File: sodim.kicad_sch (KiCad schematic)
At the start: 2 parts

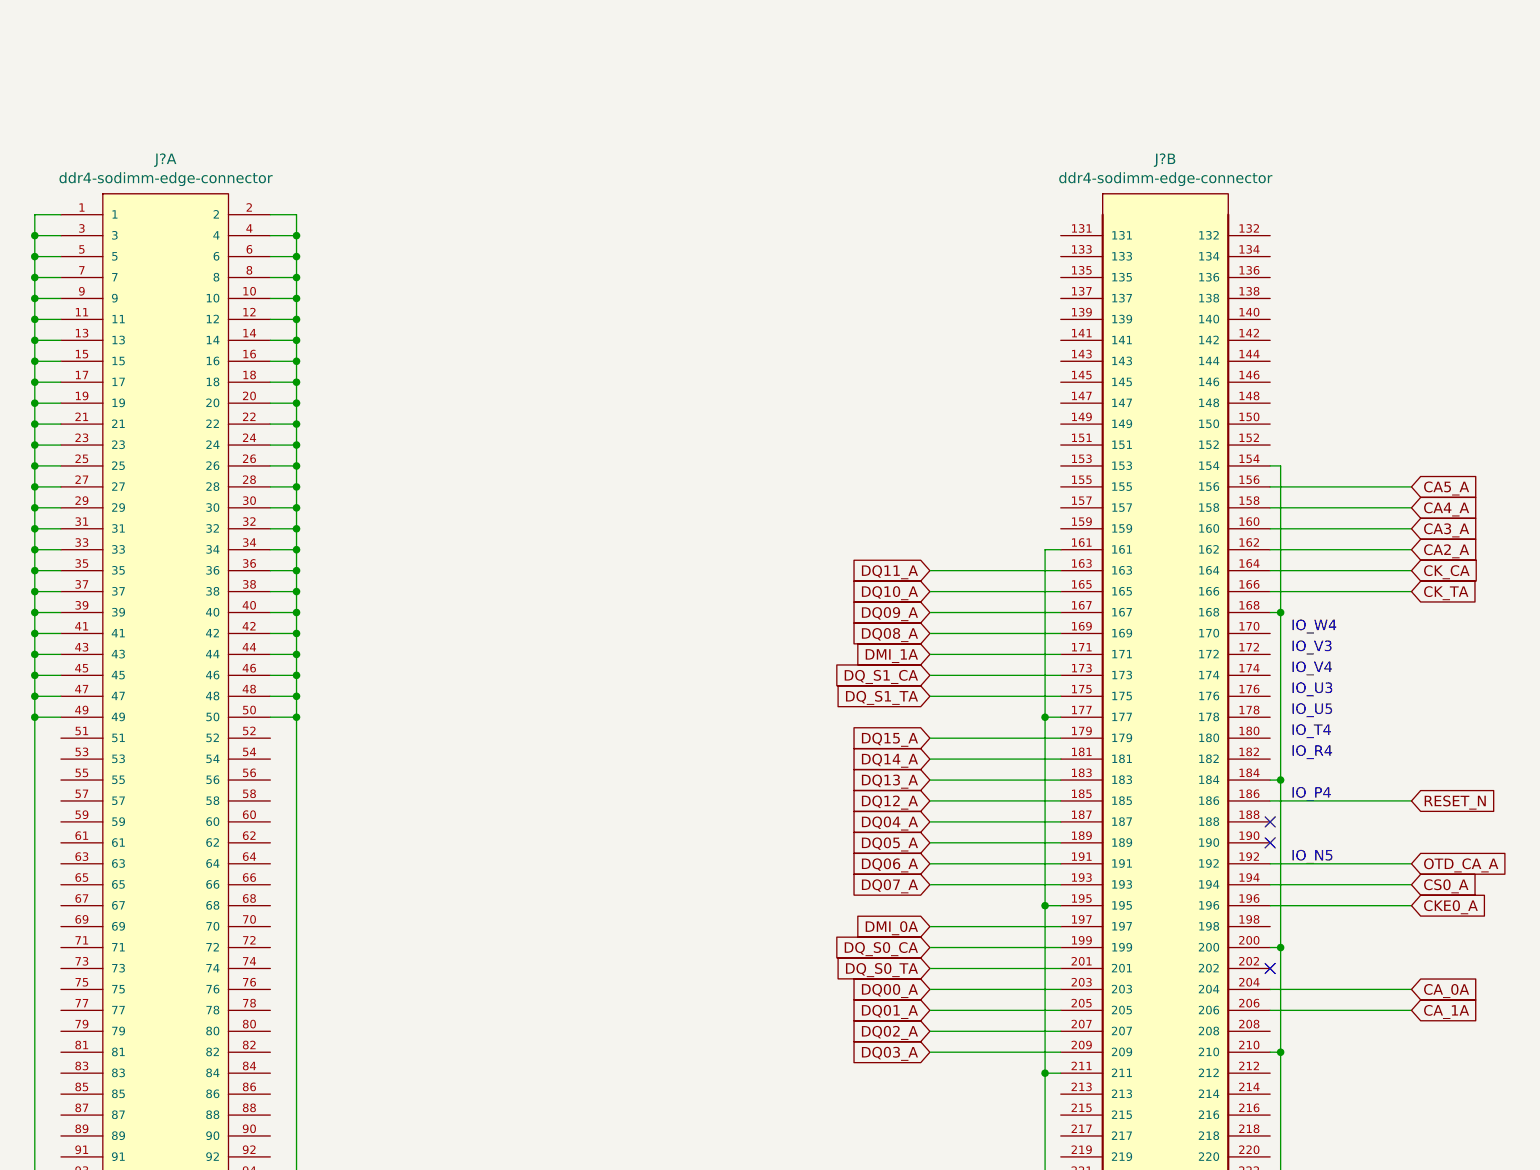
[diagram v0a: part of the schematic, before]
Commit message: Fix net names
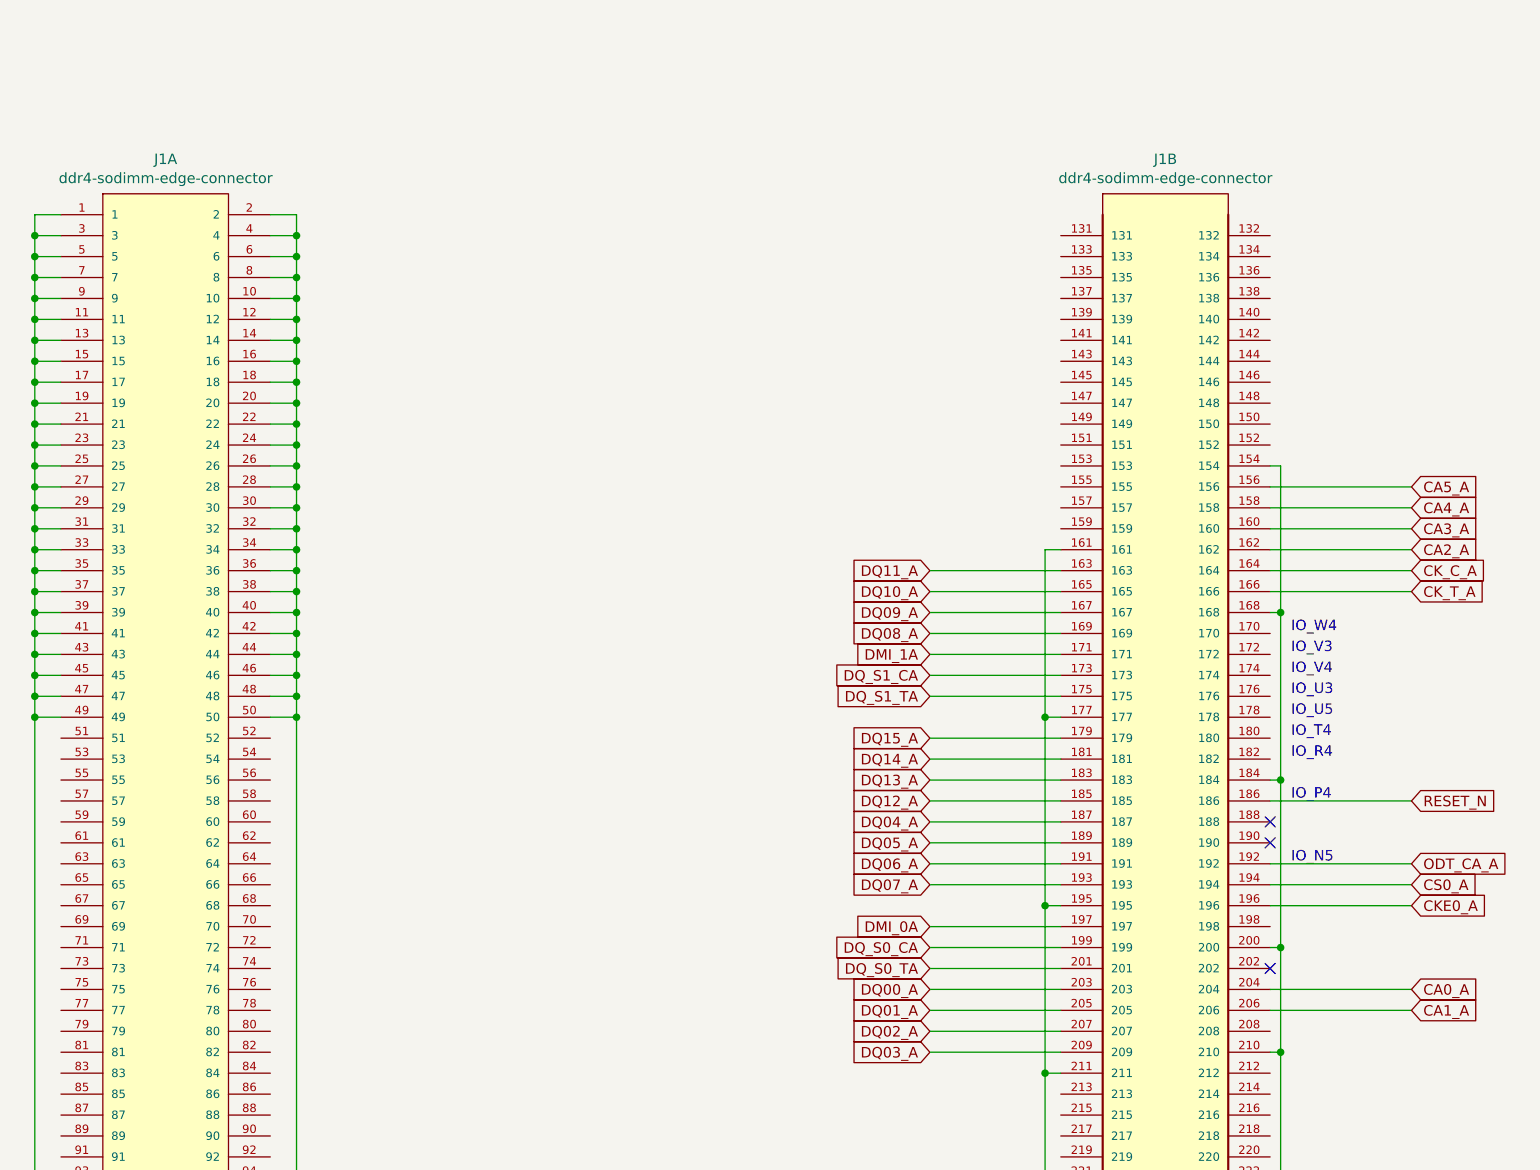
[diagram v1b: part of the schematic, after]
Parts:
- gave numbers to parts that had none: 1
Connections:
- net CA_0A renamed CA0_A
- net CA_1A renamed CA1_A
- net CK_CA renamed CK_C_A
- net CK_TA renamed CK_T_A
- net OTD_CA_A renamed ODT_CA_A

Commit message: Fix missing global links (wip), designators fixed
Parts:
- removed J1: ddr4-sodimm-edge-connector, lpddr4-testbed-footprints:SODIMM_DDR4_EDGE, symbol lpddr4-testbed:ddr4-sodimm-edge-connector
- added J1: Bus_DDR4_Edge_Conn, antmicro-footprints:Bus_DDR4_Conn_Edge, symbol antmicroMemoryConnectorsPCCardSockets:Bus_DDR4_Edge_Conn
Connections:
- net CA0_A: now also J1.204
- net CA1_A: now also J1.206
- net CA2_A: now also J1.162
- net CA3_A: now also J1.160
- net CA4_A: now also J1.158
- net CA5_A: now also J1.156
- net CKE0_A: now also J1.196
- net CK_C_A: now also J1.164
- net CK_T_A: now also J1.166
- net CS0_A: now also J1.194
- net DMI_0A: now also J1.197
- net DMI_1A: now also J1.171
- net DQ00_A: now also J1.203
- net DQ01_A: now also J1.205
- net DQ02_A: now also J1.207
- net DQ03_A: now also J1.209
- net DQ04_A: now also J1.187
- net DQ05_A: now also J1.189
- net DQ06_A: now also J1.191
- net DQ07_A: now also J1.193
- net DQ08_A: now also J1.169
- net DQ09_A: now also J1.167
- net DQ10_A: now also J1.165
- net DQ11_A: now also J1.163
- net DQ12_A: now also J1.185
- net DQ13_A: now also J1.183
- net DQ14_A: now also J1.181
- net DQ15_A: now also J1.179
- net DQ_S0_CA: now also J1.199
- net DQ_S0_TA: now also J1.201
- net DQ_S1_CA: now also J1.173
- net DQ_S1_TA: now also J1.175
- net GND: now also J1.1, J1.10, J1.11, J1.12, J1.13, J1.14, J1.15, J1.154, J1.16, J1.161, J1.168, J1.17, J1.177, J1.18, J1.184, J1.19, J1.195, J1.2, J1.20, J1.200, J1.21, J1.210, J1.211, J1.22, J1.23, J1.24, J1.25, J1.26, J1.27, J1.28, J1.29, J1.3, J1.30, J1.31, J1.32, J1.33, J1.34, J1.35, J1.36, J1.37, J1.38, J1.39, J1.4, J1.40, J1.41, J1.42, J1.43, J1.44, J1.45, J1.46, J1.47, J1.48, J1.49, J1.5, J1.50, J1.6, J1.7, J1.8, J1.9
- net ODT_CA_A: now also J1.192
- net RESET_N: now also J1.186
- net SCL: now also J1.129
- net SDA: now also J1.127
- net VDD1: now also J1.116, J1.118, J1.120, J1.122, J1.124
- net VDD2: now also J1.101, J1.103, J1.105, J1.107, J1.93, J1.95, J1.97, J1.99
- net VDDQ: now also J1.126, J1.128, J1.130, J1.246, J1.248, J1.250

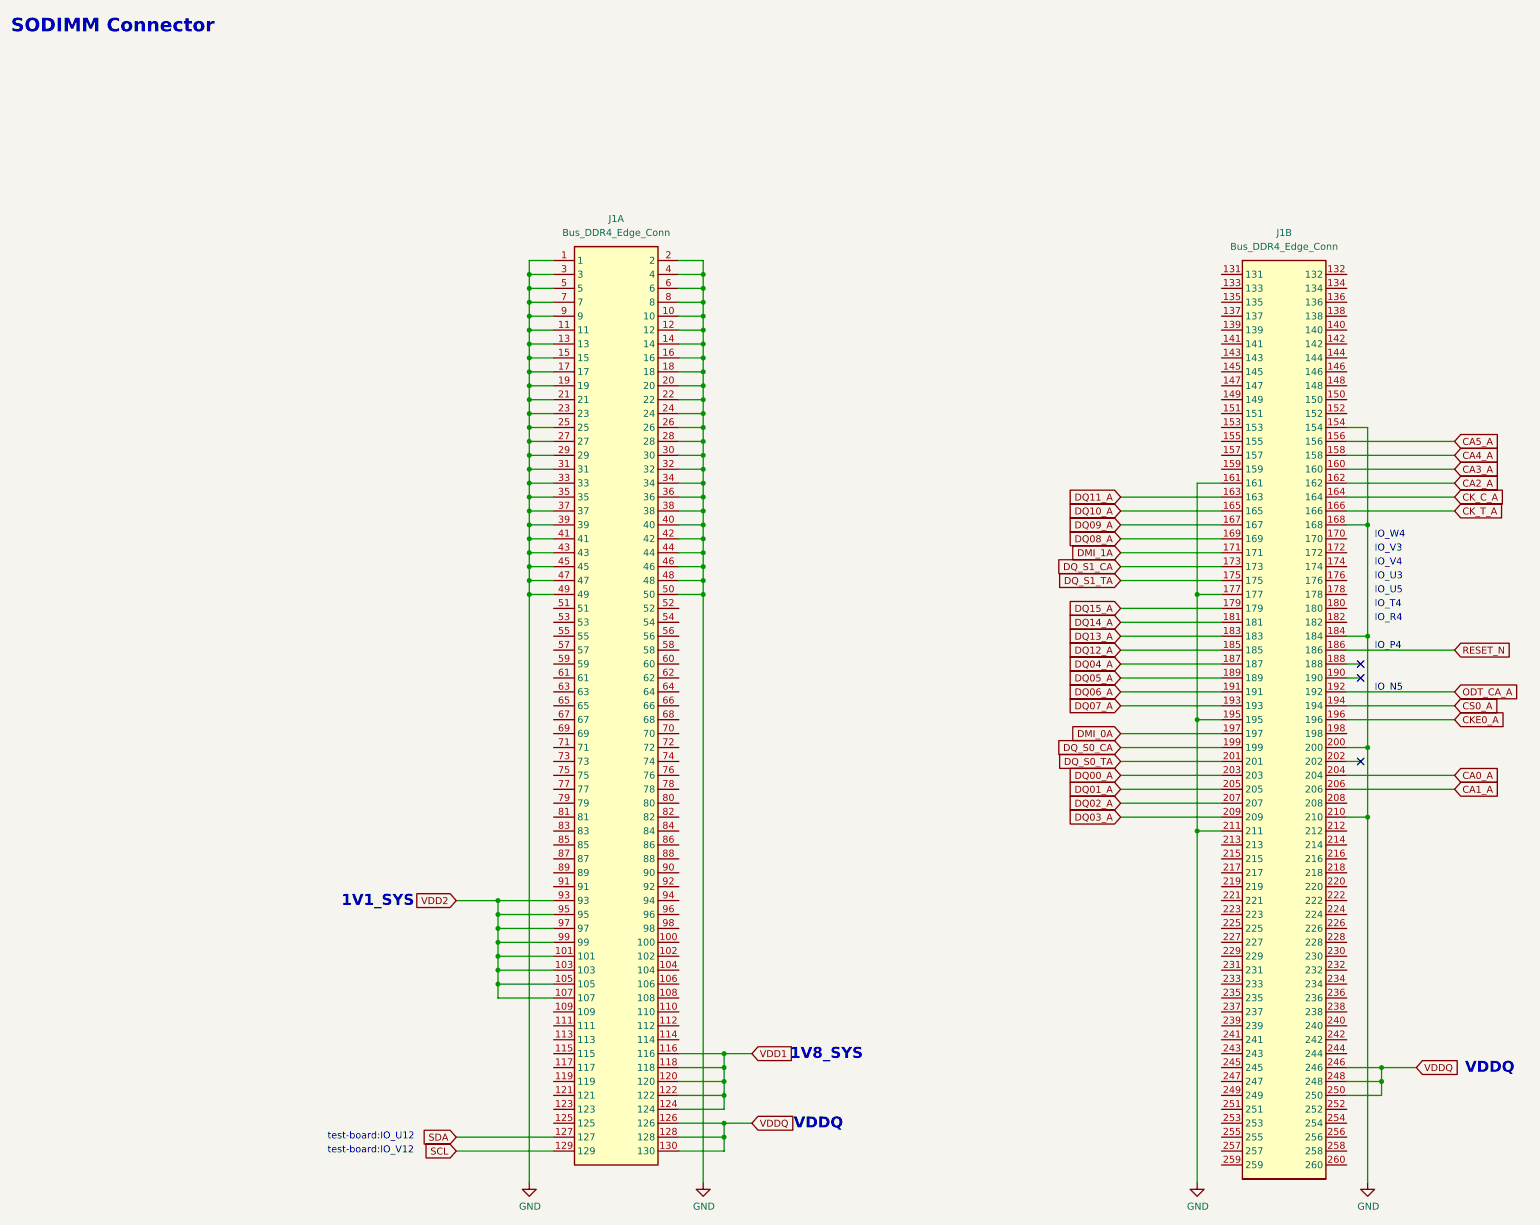
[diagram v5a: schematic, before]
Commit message: Introduce component standardization
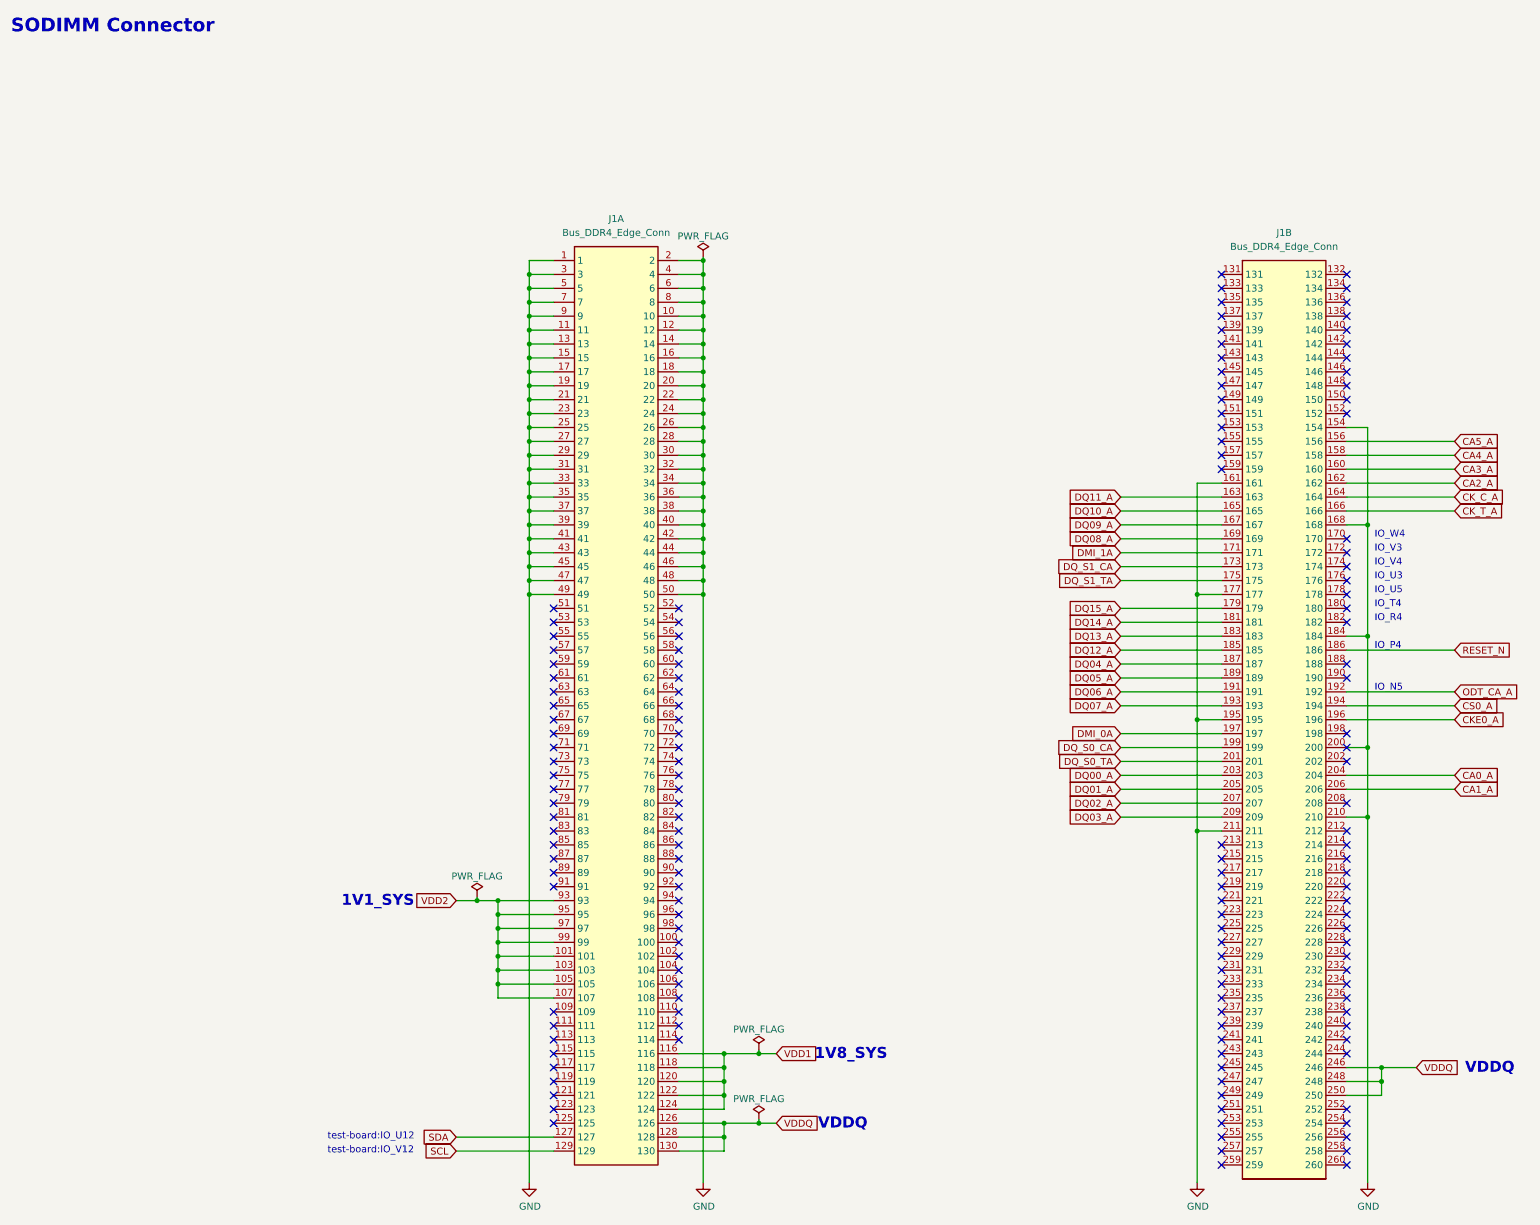
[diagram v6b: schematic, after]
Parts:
- J1: footprint antmicro-footprints:Bus_DDR4_Conn_Edge -> lpddr4-testbed-footprints:Bus_DDR4_Conn_Edge; symbol antmicroMemoryConnectorsPCCardSockets:Bus_DDR4_Edge_Conn -> lpddr4-testbed:Bus_DDR4_Edge_Conn
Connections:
- no-connect marks 3 -> 147
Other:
- title: (none) -> LPDDR4 testbed

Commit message: [#56947] Correct component references
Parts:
- J1: footprint lpddr4-testbed-footprints:Bus_DDR4_Conn_Edge -> antmicro-footprints:Edge_Conn_Bus_DDR4; symbol lpddr4-testbed:Bus_DDR4_Edge_Conn -> antmicroMemoryConnectorsPCCardSockets:Edge_Conn_Bus_DDR4; now left out of the parts list

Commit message: [#56947] Loclib
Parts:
- J1: footprint antmicro-footprints:Edge_Conn_Bus_DDR4 -> lpddr4-testbed-footprints:Edge_Conn_Bus_DDR4; symbol antmicroMemoryConnectorsPCCardSockets:Edge_Conn_Bus_DDR4 -> lpddr4-testbed:Edge_Conn_Bus_DDR4
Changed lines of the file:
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@@
     )
   )
-  (symbol (lib_id "antmicropower:GND") (at 149.225 231.775 0) (unit 1)
+  (symbol (lib_id "lpddr4-testbed:GND") (at 149.225 231.775 0) (unit 1)
     (in_bom yes) (on_board yes) (dnp no)
     (property "Reference" "#PWR0101" (at 149.225 238.125 0)
@@
     )
   )
-  (symbol (lib_id "antmicropower:GND") (at 117.475 231.775 0) (unit 1)
+  (symbol (lib_id "lpddr4-testbed:GND") (at 117.475 231.775 0) (unit 1)
     (in_bom yes) (on_board yes) (dnp no)
     (property "Reference" "#PWR0103" (at 117.475 238.125 0)
@@
     )
   )
-  (symbol (lib_id "antmicropower:GND") (at 239.395 231.775 0) (unit 1)
+  (symbol (lib_id "lpddr4-testbed:GND") (at 239.395 231.775 0) (unit 1)
     (in_bom yes) (on_board yes) (dnp no)
     (property "Reference" "#PWR0102" (at 239.395 238.125 0)
@@
     )
   )
-  (symbol (lib_id "antmicropower:GND") (at 270.51 231.775 0) (unit 1)
+  (symbol (lib_id "lpddr4-testbed:GND") (at 270.51 231.775 0) (unit 1)
     (in_bom yes) (on_board yes) (dnp no)
     (property "Reference" "#PWR0104" (at 270.51 238.125 0)
@@
     )
   )
-  (symbol (lib_id "antmicroMemoryConnectorsPCCardSockets:Edge_Conn_Bus_DDR4") (at 121.92 63.5 0) (unit 1)
+  (symbol (lib_id "lpddr4-testbed:Edge_Conn_Bus_DDR4") (at 121.92 63.5 0) (unit 1)
     (in_bom no) (on_board yes) (dnp no) (fields_autoplaced)
     (property "Reference" "J1" (at 133.35 55.88 0)
@@
       (effects (font (size 1.27 1.27) (thickness 0.15)))
     )
-    (property "Footprint" "antmicro-footprints:Edge_Conn_Bus_DDR4" (at 158.75 68.58 0)
+    (property "Footprint" "lpddr4-testbed-footprints:Edge_Conn_Bus_DDR4" (at 158.75 68.58 0)
       (effects (font (size 1.27 1.27) (thickness 0.15)) (justify left bottom) hide)
     )
@@
     )
   )
-  (symbol (lib_id "antmicropower:PWR_FLAG") (at 107.95 179.705 0) (unit 1)
+  (symbol (lib_id "lpddr4-testbed:PWR_FLAG") (at 107.95 179.705 0) (unit 1)
     (in_bom yes) (on_board yes) (dnp no)
     (property "Reference" "#FLG0104" (at 107.95 177.8 0)
@@
     )
   )
-  (symbol (lib_id "antmicropower:PWR_FLAG") (at 159.385 207.645 0) (unit 1)
+  (symbol (lib_id "lpddr4-testbed:PWR_FLAG") (at 159.385 207.645 0) (unit 1)
     (in_bom yes) (on_board yes) (dnp no)
     (property "Reference" "#FLG0102" (at 159.385 205.74 0)
@@
     )
   )
-  (symbol (lib_id "antmicropower:PWR_FLAG") (at 149.225 62.865 0) (unit 1)
+  (symbol (lib_id "lpddr4-testbed:PWR_FLAG") (at 149.225 62.865 0) (unit 1)
     (in_bom yes) (on_board yes) (dnp no)
     (property "Reference" "#FLG0103" (at 149.225 60.96 0)
@@
     )
   )
-  (symbol (lib_id "antmicropower:PWR_FLAG") (at 159.385 220.345 0) (unit 1)
+  (symbol (lib_id "lpddr4-testbed:PWR_FLAG") (at 159.385 220.345 0) (unit 1)
     (in_bom yes) (on_board yes) (dnp no)
     (property "Reference" "#FLG0101" (at 159.385 218.44 0)
@@
     )
   )
-  (symbol (lib_id "antmicroMemoryConnectorsPCCardSockets:Edge_Conn_Bus_DDR4") (at 243.84 66.04 0) (unit 2)
+  (symbol (lib_id "lpddr4-testbed:Edge_Conn_Bus_DDR4") (at 243.84 66.04 0) (unit 2)
     (in_bom no) (on_board yes) (dnp no) (fields_autoplaced)
     (property "Reference" "J1" (at 255.27 58.42 0)
@@
       (effects (font (size 1.27 1.27) (thickness 0.15)))
     )
-    (property "Footprint" "antmicro-footprints:Edge_Conn_Bus_DDR4" (at 280.67 71.12 0)
+    (property "Footprint" "lpddr4-testbed-footprints:Edge_Conn_Bus_DDR4" (at 280.67 71.12 0)
       (effects (font (size 1.27 1.27) (thickness 0.15)) (justify left bottom) hide)
     )
